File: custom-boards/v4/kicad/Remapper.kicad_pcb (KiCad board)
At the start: 2 copper layers, 91 x 37 mm, 46 parts, among them J1 AudioJack3, J2 AudioJack3, J3 AudioJack3, J4 AudioJack3, J5 AudioJack3, J6 AudioJack3, J7 AudioJack3, J8 AudioJack3, SW102 SW_Push, U103 RP2040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

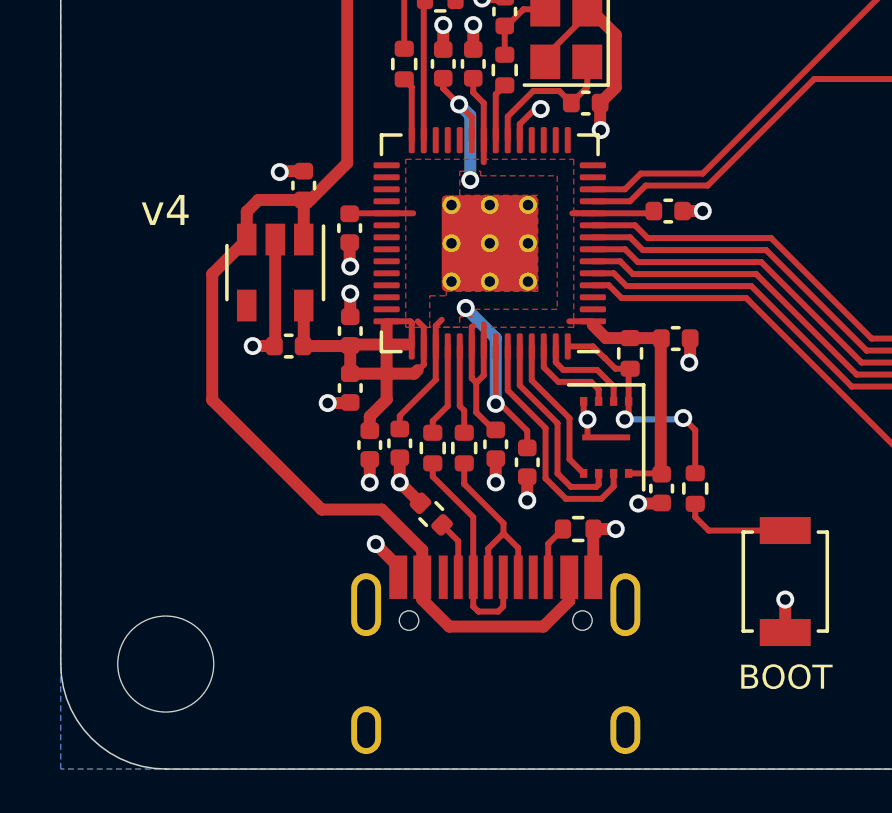
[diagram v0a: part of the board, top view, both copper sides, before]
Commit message: Update custom boards
This commit makes the following changes to the custom PCB designs.

v1-v5: flash chip footprint changed, previous one caused issues in
manufacturing. Some other components moved around as a result.

v1-v5: flash chip changed from 1 megabyte to 2 megabyte one.

v1: USB Type A port component changed, previous one was consistently
soldered on crooked by JLCPCB.

The new designs are named v1.1-v5.1.

Schematics and enclosure files are unchanged.
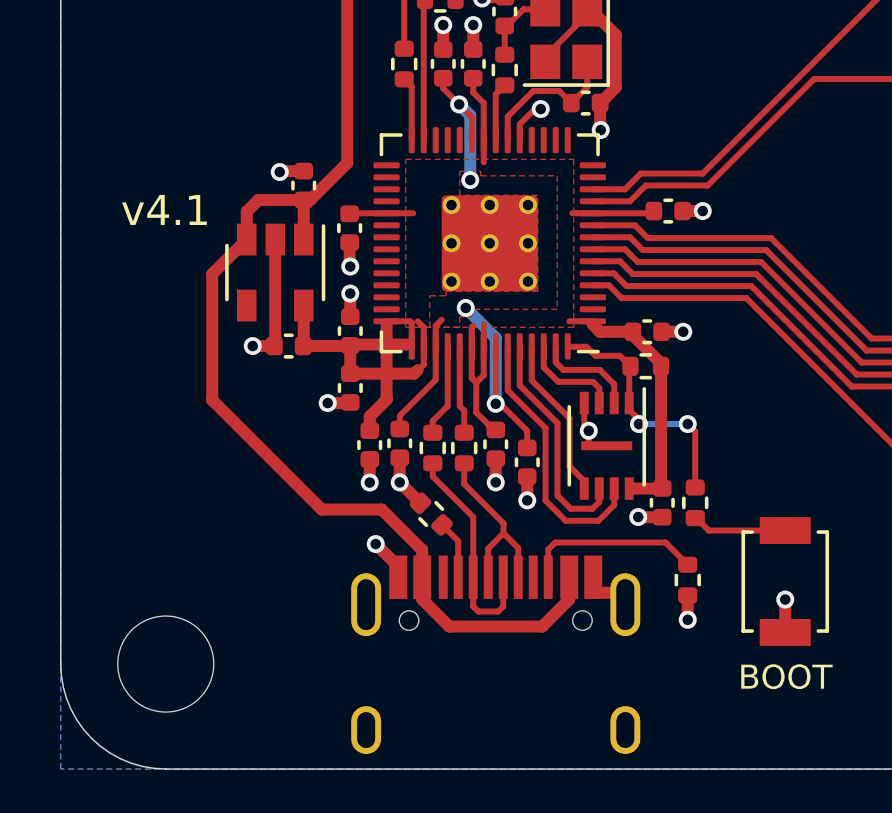
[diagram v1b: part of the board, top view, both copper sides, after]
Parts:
- moved R3 4.03 mm to (152.9, 58.8), turned to -90 degrees
- moved C104 0.98 mm to (151.6, 50.5)
- moved R105 0.67 mm to (151.5, 51.7), turned to 180 degrees
- moved C117 0.48 mm to (152.1, 56.2)
- moved R106 0.48 mm to (153.2, 56.2)
- moved U105 0.28 mm to (150.2, 54.3)
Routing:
- net Net-(USB2-CC2): track 1.81 -> 5.98 mm
- net 1QSPI_SD3: track 8.08 -> 9.00 mm
- net 1QSPI_SCLK: track 6.72 -> 7.61 mm
- net 1QSPI_SD0: track 4.95 -> 5.46 mm
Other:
- board text added: "v4.1"
- board text removed: "v4"
